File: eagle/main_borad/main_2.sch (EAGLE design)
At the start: 24 parts, among them Q2 BSS123, Q3 BSS123, Q5 BSS123, Q6 BSS123, U1 XMEGA-A4TQFP

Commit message: Druha verze navrhu desek pro rizeni podvozku.
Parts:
- added JP7: (no value), pinhead:PINHD-1X1
- added LED2, LED3, LED4, LED5: (no value), SparkFun-LED:LED1206
- added R1, R12, R13, R14: 220, eagle-ltspice:RR1206
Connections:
- new net N$21: R1.1, U1.PA3(ADC3)
- new net N$22: R12.1, U1.PA2(ADC2)
- new net N$23: R13.1, U1.PA1(ADC1)
- new net N$24: R14.1, U1.PA0(ADC0/AREF)
- new net N$25: LED5.A, R1.2
- new net N$26: LED2.A, R12.2
- new net N$27: LED3.A, R13.2
- new net N$28: LED4.A, R14.2
- net GND: now also LED2.C, LED3.C, LED4.C, LED5.C
- net N$3: no longer U1.PA0(ADC0/AREF), U1.PA1(ADC1), U1.PA2(ADC2), U1.PA3(ADC3)
- net RESET: now also JP7.1
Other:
- moved on the sheet: R11

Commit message: main_board PCB
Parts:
- removed R11: 10k, eagle-ltspice:RR1206
- added JP10: (no value), pinhead:PINHD-1X4
- added JP8, JP9: (no value), pinhead:PINHD-1X2
- C2, C3, C4: device eagle-ltspice:CC1206 -> eagle-ltspice:C
- R1, R10, R12, R13, R14, R2, R3, R4, R5, R6, R7, R8, R9: device eagle-ltspice:RR1206 -> eagle-ltspice:R
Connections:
- removed net N$3: R11.1, U1.PA4(ADC4), U1.PA5(ADC5), U1.PA6(ADC6), U1.PA7/(ADC7/AC0-OUT), U1.PB0(ADC8/AREF), U1.PB1(ADC9), U1.PB2(ADC10/DAC0), U1.PB3(ADC11/DAC1), U1.PC2(OC0C/RXD0), U1.PC3(OC0D/TXD0), U1.PC4(OC1A/!SS!), U1.PD0(OC0A), U1.PE2(OC0C/RXD0), U1.PE3(OC0D/TXD0), U1.PR0(XTAL2/TOSC1), U1.PR1(XTAL1/TOSC1)
- net GND: now also JP10.1, JP8.1, JP9.1, U1.PA4(ADC4), U1.PA5(ADC5), U1.PA6(ADC6), U1.PA7/(ADC7/AC0-OUT), U1.PB0(ADC8/AREF), U1.PB1(ADC9), U1.PB2(ADC10/DAC0), U1.PB3(ADC11/DAC1), U1.PC2(OC0C/RXD0), U1.PC3(OC0D/TXD0), U1.PC4(OC1A/!SS!), U1.PD0(OC0A), U1.PE2(OC0C/RXD0), U1.PE3(OC0D/TXD0), U1.PR0(XTAL2/TOSC1), U1.PR1(XTAL1/TOSC1)
- net N$15: now also JP4.3; no longer JP4.2
- net N$18: now also JP5.2; no longer JP5.3
- net N$20: now also JP5.3; no longer JP5.2
- net N$9: now also JP4.2; no longer JP4.3
- net SCL0: now also JP10.3
- net SCL1: now also JP3.3; no longer JP3.4
- net SDA0: now also JP10.2
- net SDA1: now also JP3.2; no longer JP3.3
- net VCC: now also JP10.4, JP3.4, JP8.2, JP9.2; no longer JP3.2, R11.2

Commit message: main_board, ver 3.0
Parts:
- removed JP9: (no value), pinhead:PINHD-1X2
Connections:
- net GND: no longer JP9.1
- net VCC: no longer JP9.2
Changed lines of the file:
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@@
 <part name="P+1" library="supply1" deviceset="VCC" device=""/>
 <part name="GND7" library="supply1" deviceset="GND" device=""/>
-<part name="JP9" library="pinhead" deviceset="PINHD-1X2" device=""/>
-<part name="P+12" library="supply1" deviceset="VCC" device=""/>
-<part name="GND8" library="supply1" deviceset="GND" device=""/>
 <part name="JP10" library="pinhead" deviceset="PINHD-1X4" device=""/>
 <part name="GND9" library="supply1" deviceset="GND" device=""/>
@@
 <instance part="P+1" gate="VCC" x="50.8" y="-17.78" rot="R90"/>
 <instance part="GND7" gate="1" x="50.8" y="-15.24" rot="R270"/>
-<instance part="JP9" gate="G$1" x="68.58" y="-2.54"/>
-<instance part="P+12" gate="VCC" x="50.8" y="-2.54" rot="R90"/>
-<instance part="GND8" gate="1" x="50.8" y="0" rot="R270"/>
 <instance part="JP10" gate="A" x="167.64" y="127" rot="R90"/>
 <instance part="GND9" gate="1" x="149.86" y="114.3" rot="R270"/>
@@
 <wire x1="66.04" y1="-17.78" x2="53.34" y2="-17.78" width="0.1524" layer="91"/>
 <pinref part="P+1" gate="VCC" pin="VCC"/>
-</segment>
-<segment>
-<pinref part="JP9" gate="G$1" pin="2"/>
-<wire x1="66.04" y1="-2.54" x2="53.34" y2="-2.54" width="0.1524" layer="91"/>
-<pinref part="P+12" gate="VCC" pin="VCC"/>
 </segment>
 <segment>
@@
 </segment>
 <segment>
-<pinref part="JP9" gate="G$1" pin="1"/>
-<wire x1="66.04" y1="0" x2="53.34" y2="0" width="0.1524" layer="91"/>
-<pinref part="GND8" gate="1" pin="GND"/>
-</segment>
-<segment>

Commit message: PCB layout 6.0
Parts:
- JP10: device pinhead:PINHD-1X4 -> pinhead:PINHD-1X5
- JP8: device pinhead:PINHD-1X2 -> pinhead:PINHD-1X3
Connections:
- net VCC: now also JP10.5, JP8.3
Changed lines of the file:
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@@
 <part name="JP7" library="pinhead" deviceset="PINHD-1X1" device=""/>
 <part name="GND6" library="supply1" deviceset="GND" device=""/>
-<part name="JP8" library="pinhead" deviceset="PINHD-1X2" device=""/>
+<part name="JP8" library="pinhead" deviceset="PINHD-1X3" device=""/>
 <part name="P+1" library="supply1" deviceset="VCC" device=""/>
 <part name="GND7" library="supply1" deviceset="GND" device=""/>
-<part name="JP10" library="pinhead" deviceset="PINHD-1X4" device=""/>
+<part name="JP10" library="pinhead" deviceset="PINHD-1X5" device=""/>
 <part name="GND9" library="supply1" deviceset="GND" device=""/>
 <part name="P+13" library="supply1" deviceset="VCC" device=""/>
@@
 <instance part="JP7" gate="G$1" x="-27.94" y="35.56" rot="R180"/>
 <instance part="GND6" gate="1" x="45.72" y="119.38" rot="R180"/>
-<instance part="JP8" gate="G$1" x="68.58" y="-17.78"/>
+<instance part="JP8" gate="A" x="68.58" y="-17.78"/>
 <instance part="P+1" gate="VCC" x="50.8" y="-17.78" rot="R90"/>
 <instance part="GND7" gate="1" x="50.8" y="-15.24" rot="R270"/>
@@
 </segment>
 <segment>
-<pinref part="JP8" gate="G$1" pin="2"/>
+<pinref part="JP8" gate="A" pin="2"/>
 <wire x1="66.04" y1="-17.78" x2="53.34" y2="-17.78" width="0.1524" layer="91"/>
 <pinref part="P+1" gate="VCC" pin="VCC"/>
+<wire x1="66.04" y1="-17.78" x2="60.96" y2="-17.78" width="0.1524" layer="91"/>
+<wire x1="60.96" y1="-17.78" x2="60.96" y2="-20.32" width="0.1524" layer="91"/>
+<pinref part="JP8" gate="A" pin="3"/>
+<wire x1="60.96" y1="-20.32" x2="66.04" y2="-20.32" width="0.1524" layer="91"/>
 </segment>
 <segment>
 <pinref part="JP10" gate="A" pin="4"/>
-<wire x1="170.18" y1="124.46" x2="170.18" y2="109.22" width="0.1524" layer="91"/>
+<wire x1="170.18" y1="121.92" x2="170.18" y2="109.22" width="0.1524" layer="91"/>
 <wire x1="170.18" y1="109.22" x2="152.4" y2="109.22" width="0.1524" layer="91"/>
 <pinref part="P+13" gate="VCC" pin="VCC"/>
+<wire x1="170.18" y1="124.46" x2="170.18" y2="121.92" width="0.1524" layer="91"/>
+<wire x1="170.18" y1="121.92" x2="172.72" y2="121.92" width="0.1524" layer="91"/>
+<pinref part="JP10" gate="A" pin="5"/>
+<wire x1="172.72" y1="121.92" x2="172.72" y2="124.46" width="0.1524" layer="91"/>
 </segment>
 </net>
@@
 </segment>
 <segment>
-<pinref part="JP8" gate="G$1" pin="1"/>
+<pinref part="JP8" gate="A" pin="1"/>
 <wire x1="66.04" y1="-15.24" x2="53.34" y2="-15.24" width="0.1524" layer="91"/>
 <pinref part="GND7" gate="1" pin="GND"/>

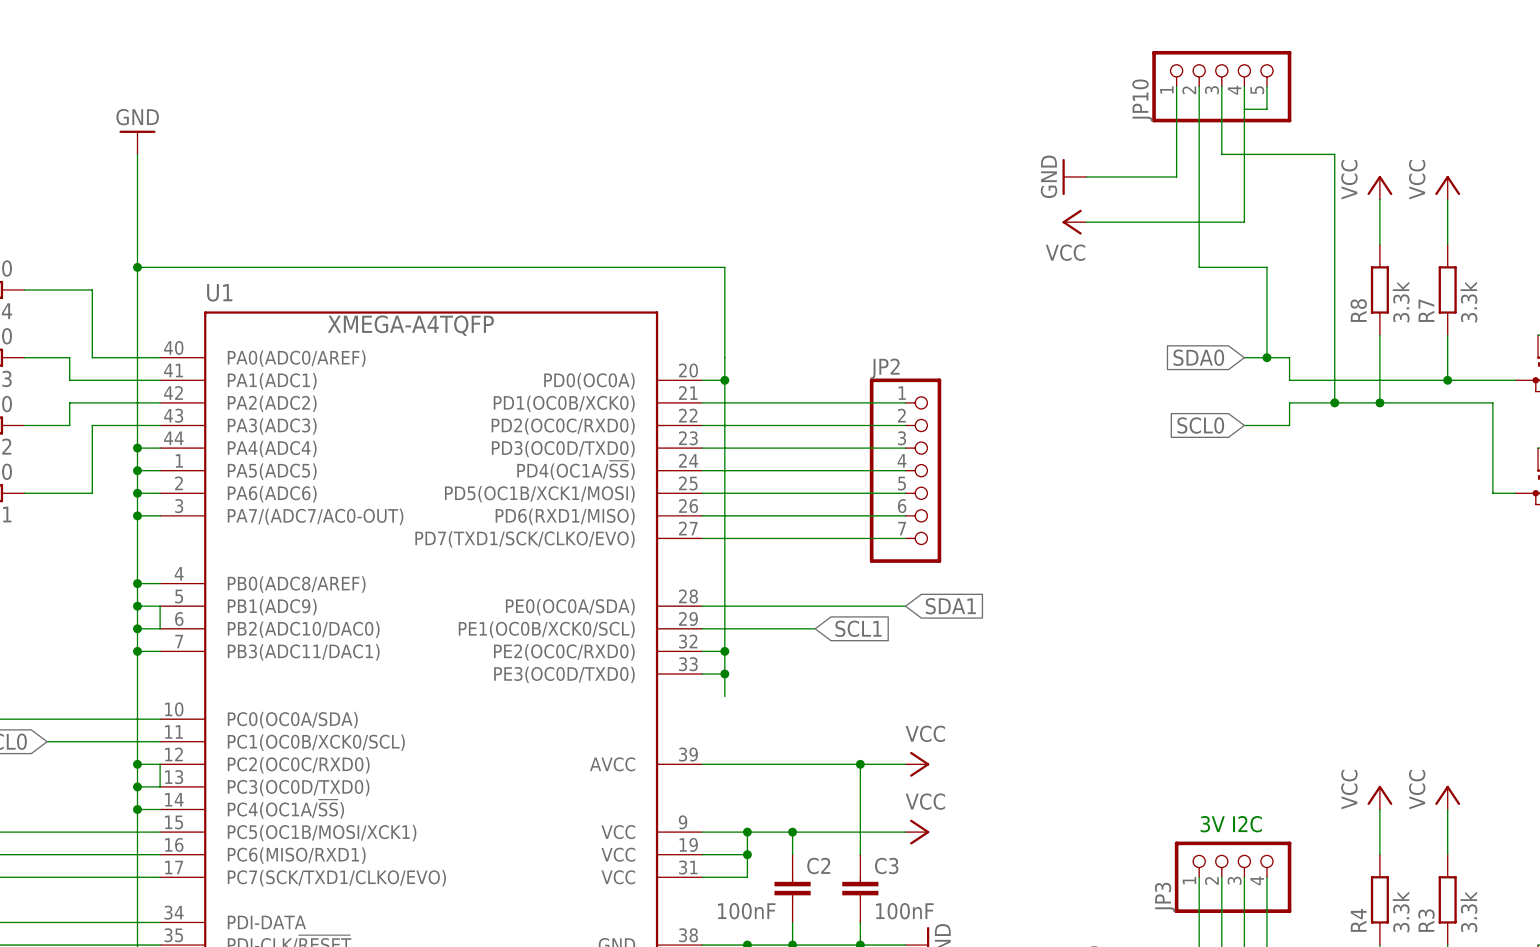
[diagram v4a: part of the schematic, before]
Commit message: motor_drivers updated
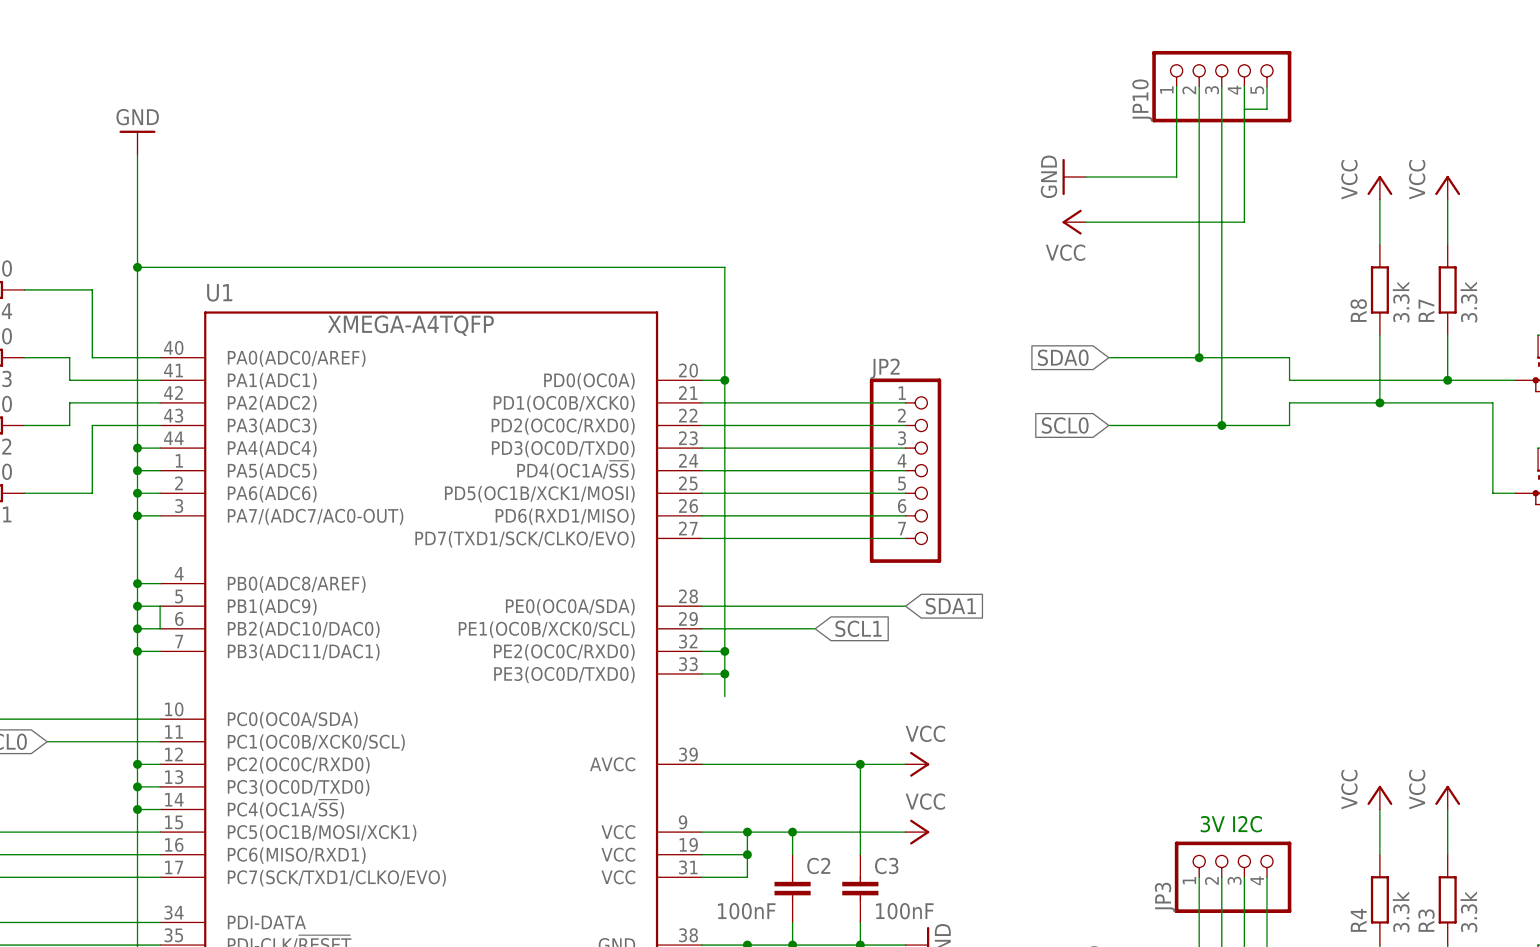
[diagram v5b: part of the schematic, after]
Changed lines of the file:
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@@
 <pinref part="U1" gate="G$1" pin="PC2(OC0C/RXD0)"/>
 <wire x1="45.72" y1="45.72" x2="48.26" y2="45.72" width="0.1524" layer="91"/>
-<wire x1="48.26" y1="45.72" x2="48.26" y2="48.26" width="0.1524" layer="91"/>
 <wire x1="48.26" y1="48.26" x2="45.72" y2="48.26" width="0.1524" layer="91"/>
 <pinref part="U1" gate="G$1" pin="PB3(ADC11/DAC1)"/>
@@
 <pinref part="GND6" gate="1" pin="GND"/>
 <wire x1="45.72" y1="104.14" x2="111.76" y2="104.14" width="0.1524" layer="91"/>
-<wire x1="111.76" y1="104.14" x2="111.76" y2="93.98" width="0.1524" layer="91"/>
+<wire x1="111.76" y1="104.14" x2="111.76" y2="91.44" width="0.1524" layer="91"/>
 <pinref part="U1" gate="G$1" pin="PE3(OC0D/TXD0)"/>
 <wire x1="111.76" y1="91.44" x2="111.76" y2="60.96" width="0.1524" layer="91"/>
@@
 <pinref part="U1" gate="G$1" pin="PD0(OC0A)"/>
 <wire x1="109.22" y1="91.44" x2="111.76" y2="91.44" width="0.1524" layer="91"/>
-<wire x1="111.76" y1="91.44" x2="111.76" y2="93.98" width="0.1524" layer="91"/>
 <junction x="111.76" y="58.42"/>
 <junction x="111.76" y="60.96"/>
@@
 <pinref part="R8" gate="G$1" pin="1"/>
 <wire x1="185.42" y1="96.52" x2="185.42" y2="88.9" width="0.1524" layer="91"/>
-<label x="170.18" y="86.36" size="1.778" layer="95" rot="R180" xref="yes"/>
-<wire x1="185.42" y1="88.9" x2="180.34" y2="88.9" width="0.1524" layer="91"/>
-<wire x1="180.34" y1="88.9" x2="175.26" y2="88.9" width="0.1524" layer="91"/>
+<label x="154.94" y="86.36" size="1.778" layer="95" rot="R180" xref="yes"/>
+<wire x1="185.42" y1="88.9" x2="175.26" y2="88.9" width="0.1524" layer="91"/>
 <wire x1="175.26" y1="88.9" x2="175.26" y2="86.36" width="0.1524" layer="91"/>
-<wire x1="175.26" y1="86.36" x2="170.18" y2="86.36" width="0.1524" layer="91"/>
+<wire x1="175.26" y1="86.36" x2="167.64" y2="86.36" width="0.1524" layer="91"/>
 <junction x="185.42" y="88.9"/>
 <pinref part="JP10" gate="A" pin="3"/>
-<wire x1="167.64" y1="124.46" x2="167.64" y2="116.84" width="0.1524" layer="91"/>
-<wire x1="167.64" y1="116.84" x2="180.34" y2="116.84" width="0.1524" layer="91"/>
-<wire x1="180.34" y1="116.84" x2="180.34" y2="88.9" width="0.1524" layer="91"/>
-<junction x="180.34" y="88.9"/>
+<wire x1="167.64" y1="86.36" x2="154.94" y2="86.36" width="0.1524" layer="91"/>
+<wire x1="167.64" y1="124.46" x2="167.64" y2="86.36" width="0.1524" layer="91"/>
+<junction x="167.64" y="86.36"/>
 </segment>
 </net>
@@
 <pinref part="R7" gate="G$1" pin="1"/>
 <wire x1="193.04" y1="96.52" x2="193.04" y2="91.44" width="0.1524" layer="91"/>
-<label x="170.18" y="93.98" size="1.778" layer="95" rot="R180" xref="yes"/>
+<label x="154.94" y="93.98" size="1.778" layer="95" rot="R180" xref="yes"/>
 <wire x1="193.04" y1="91.44" x2="175.26" y2="91.44" width="0.1524" layer="91"/>
 <wire x1="175.26" y1="91.44" x2="175.26" y2="93.98" width="0.1524" layer="91"/>
 <junction x="193.04" y="91.44"/>
-<wire x1="175.26" y1="93.98" x2="172.72" y2="93.98" width="0.1524" layer="91"/>
+<wire x1="175.26" y1="93.98" x2="165.1" y2="93.98" width="0.1524" layer="91"/>
 <pinref part="JP10" gate="A" pin="2"/>
-<wire x1="172.72" y1="93.98" x2="170.18" y2="93.98" width="0.1524" layer="91"/>
-<wire x1="165.1" y1="124.46" x2="165.1" y2="104.14" width="0.1524" layer="91"/>
-<wire x1="165.1" y1="104.14" x2="172.72" y2="104.14" width="0.1524" layer="91"/>
-<wire x1="172.72" y1="104.14" x2="172.72" y2="93.98" width="0.1524" layer="91"/>
-<junction x="172.72" y="93.98"/>
+<wire x1="165.1" y1="93.98" x2="154.94" y2="93.98" width="0.1524" layer="91"/>
+<wire x1="165.1" y1="124.46" x2="165.1" y2="93.98" width="0.1524" layer="91"/>
+<junction x="165.1" y="93.98"/>
 </segment>
 </net>
